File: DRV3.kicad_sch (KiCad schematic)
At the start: 15 parts

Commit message: Motor symbol corrected, Oscillator circuitry added and external footprints added
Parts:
- removed UC: DRV10970PWPR, symbol DRV10970PWPR:DRV10970PWPR
- added UA?: DRV10970PWPR, DRV10970PWPR:SOP65P640X120-25N, symbol DRV10970PWPR:DRV10970PWPR
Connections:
- net BRK_3: now also UA?.21 (BRKMOD)
- net CMT_3: now also UA?.20 (CMTMOD)
- net CPN: now also UA?.10 (CPN)
- net CPP: now also UA?.9 (CPP)
- net CS: now also UA?.17 (CS)
- net FG_3: now also UA?.24 (FG)
- net FR_3: now also UA?.23 (FR)
- net GND: now also UA?.12 (GND), UA?.25 (EP)
- net MOT_POW: now also UA?.15 (VM)
- net MOT_PWM_3: now also UA?.19 (PWM)
- net RD_3: now also UA?.18 (RD)
- net RTRY: now also UA?.22 (RETRY)
- net U_3: now also UA?.14 (U)
- net U_HP_3: now also UA?.2 (U_HP)
- net VCP: now also UA?.8 (VCP)
- net VINT: now also UA?.16 (VINT)
- net VINT_BY_2: now also UA?.3 (U_HN), UA?.5 (V_HN), UA?.7 (W_HN)
- net V_3: now also UA?.13 (V)
- net V_HP_3: now also UA?.4 (V_HP)
- net W_3: now also UA?.11 (W)
- net W_HP_3: now also UA?.6 (W_HP)
- net at TPC1.1: now also UA?.1 (DAA)
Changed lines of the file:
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@@
   (symbol (lib_id "power:GND") (at 181.61 109.22 0) (unit 1)
     (in_bom yes) (on_board yes) (fields_autoplaced)
-    (property "Reference" "#PWR?" (id 0) (at 181.61 115.57 0)
+    (property "Reference" "#PWR0193" (id 0) (at 181.61 115.57 0)
       (effects (font (size 1.27 1.27)) hide)
     )
@@
   (symbol (lib_id "power:GND") (at 215.9 139.7 0) (unit 1)
     (in_bom yes) (on_board yes) (fields_autoplaced)
-    (property "Reference" "#PWR?" (id 0) (at 215.9 146.05 0)
+    (property "Reference" "#PWR0191" (id 0) (at 215.9 146.05 0)
       (effects (font (size 1.27 1.27)) hide)
     )
@@
     (pin "2")
   )
+  (symbol (lib_id "power:GND") (at 198.12 101.6 0) (unit 1)
+    (in_bom yes) (on_board yes) (fields_autoplaced)
+    (property "Reference" "#PWR0192" (id 0) (at 198.12 107.95 0)
+      (effects (font (size 1.27 1.27)) hide)
+    )
+    (property "Value" "GND" (id 1) (at 198.12 106.68 0))
+    (property "Footprint" "" (id 2) (at 198.12 101.6 0)
+      (effects (font (size 1.27 1.27)) hide)
+    )
+    (property "Datasheet" "" (id 3) (at 198.12 101.6 0)
+      (effects (font (size 1.27 1.27)) hide)
+    )
+    (pin "1")
+  )
+  (symbol (lib_id "Device:R") (at 198.12 90.17 0) (unit 1)
+    (in_bom yes) (on_board yes) (fields_autoplaced)
+    (property "Reference" "RC6" (id 0) (at 200.66 88.8999 0)
+      (effects (font (size 1.27 1.27)) (justify left))
+    )
+    (property "Value" "22K" (id 1) (at 200.66 91.4399 0)
+      (effects (font (size 1.27 1.27)) (justify left))
+    )
+    (property "Footprint" "" (id 2) (at 196.342 90.17 90)
+      (effects (font (size 1.27 1.27)) hide)
+    )
+    (property "Datasheet" "~" (id 3) (at 198.12 90.17 0)
+      (effects (font (size 1.27 1.27)) hide)
+    )
+    (pin "1")
+    (pin "2")
+  )
+  (symbol (lib_id "power:GND") (at 130.81 104.14 0) (unit 1)
+    (in_bom yes) (on_board yes) (fields_autoplaced)
+    (property "Reference" "#PWR0188" (id 0) (at 130.81 110.49 0)
+      (effects (font (size 1.27 1.27)) hide)
+    )
+    (property "Value" "GND" (id 1) (at 130.81 109.22 0))
+    (property "Footprint" "" (id 2) (at 130.81 104.14 0)
+      (effects (font (size 1.27 1.27)) hide)
+    )
+    (property "Datasheet" "" (id 3) (at 130.81 104.14 0)
+      (effects (font (size 1.27 1.27)) hide)
+    )
+    (pin "1")
+  )
+  (symbol (lib_id "pspice:C") (at 119.38 139.7 0) (unit 1)
+    (in_bom yes) (on_board yes) (fields_autoplaced)
+    (property "Reference" "CA?" (id 0) (at 124.46 138.4299 0)
+      (effects (font (size 1.27 1.27)) (justify left))
+    )
+    (property "Value" "1u" (id 1) (at 124.46 140.9699 0)
+      (effects (font (size 1.27 1.27)) (justify left))
+    )
+    (property "Footprint" "" (id 2) (at 119.38 139.7 0)
+      (effects (font (size 1.27 1.27)) hide)
+    )
+    (property "Datasheet" "~" (id 3) (at 119.38 139.7 0)
+      (effects (font (size 1.27 1.27)) hide)
+    )
+    (pin "1")
+    (pin "2")
+  )
+  (symbol (lib_id "Device:R") (at 87.63 69.85 0) (unit 1)
+    (in_bom yes) (on_board yes) (fields_autoplaced)
+    (property "Reference" "RC1" (id 0) (at 90.17 68.5799 0)
+      (effects (font (size 1.27 1.27)) (justify left))
+    )
+    (property "Value" "4.7K" (id 1) (at 90.17 71.1199 0)
+      (effects (font (size 1.27 1.27)) (justify left))
+    )
+    (property "Footprint" "" (id 2) (at 85.852 69.85 90)
+      (effects (font (size 1.27 1.27)) hide)
+    )
+    (property "Datasheet" "~" (id 3) (at 87.63 69.85 0)
+      (effects (font (size 1.27 1.27)) hide)
+    )
+    (pin "1")
+    (pin "2")
+  )
+  (symbol (lib_id "Connector:TestPoint") (at 129.54 76.2 0) (unit 1)
+    (in_bom yes) (on_board yes) (fields_autoplaced)
+    (property "Reference" "TPC1" (id 0) (at 132.08 71.6279 0)
+      (effects (font (size 1.27 1.27)) (justify left))
+    )
+    (property "Value" "TestPoint" (id 1) (at 132.08 74.1679 0)
+      (effects (font (size 1.27 1.27)) (justify left))
+    )
+    (property "Footprint" "" (id 2) (at 134.62 76.2 0)
+      (effects (font (size 1.27 1.27)) hide)
+    )
+    (property "Datasheet" "~" (id 3) (at 134.62 76.2 0)
+      (effects (font (size 1.27 1.27)) hide)
+    )
+    (pin "1")
+  )
   (symbol (lib_id "DRV10970PWPR:DRV10970PWPR") (at 130.81 76.2 0) (unit 1)
     (in_bom yes) (on_board yes) (fields_autoplaced)
-    (property "Reference" "UC" (id 0) (at 146.05 63.5 0))
+    (property "Reference" "UA?" (id 0) (at 146.05 63.5 0))
     (property "Value" "DRV10970PWPR" (id 1) (at 146.05 66.04 0))
-    (property "Footprint" "" (id 2) (at 130.81 76.2 0)
+    (property "Footprint" "DRV10970PWPR:SOP65P640X120-25N" (id 2) (at 130.81 76.2 0)
       (effects (font (size 1.27 1.27)) hide)
     )
@@
     (pin "9")
   )
-  (symbol (lib_id "power:GND") (at 198.12 101.6 0) (unit 1)
-    (in_bom yes) (on_board yes) (fields_autoplaced)
-    (property "Reference" "#PWR?" (id 0) (at 198.12 107.95 0)
-      (effects (font (size 1.27 1.27)) hide)
-    )
-    (property "Value" "GND" (id 1) (at 198.12 106.68 0))
-    (property "Footprint" "" (id 2) (at 198.12 101.6 0)
-      (effects (font (size 1.27 1.27)) hide)
-    )
-    (property "Datasheet" "" (id 3) (at 198.12 101.6 0)
-      (effects (font (size 1.27 1.27)) hide)
-    )
-    (pin "1")
-  )
-  (symbol (lib_id "Device:R") (at 198.12 90.17 0) (unit 1)
-    (in_bom yes) (on_board yes) (fields_autoplaced)
-    (property "Reference" "RC6" (id 0) (at 200.66 88.8999 0)
-      (effects (font (size 1.27 1.27)) (justify left))
-    )
-    (property "Value" "22K" (id 1) (at 200.66 91.4399 0)
-      (effects (font (size 1.27 1.27)) (justify left))
-    )
-    (property "Footprint" "" (id 2) (at 196.342 90.17 90)
-      (effects (font (size 1.27 1.27)) hide)
-    )
-    (property "Datasheet" "~" (id 3) (at 198.12 90.17 0)
-      (effects (font (size 1.27 1.27)) hide)
-    )
-    (pin "1")
-    (pin "2")
-  )
-  (symbol (lib_id "power:GND") (at 130.81 104.14 0) (unit 1)
-    (in_bom yes) (on_board yes) (fields_autoplaced)
-    (property "Reference" "#PWR?" (id 0) (at 130.81 110.49 0)
-      (effects (font (size 1.27 1.27)) hide)
-    )
-    (property "Value" "GND" (id 1) (at 130.81 109.22 0))
-    (property "Footprint" "" (id 2) (at 130.81 104.14 0)
-      (effects (font (size 1.27 1.27)) hide)
-    )
-    (property "Datasheet" "" (id 3) (at 130.81 104.14 0)
-      (effects (font (size 1.27 1.27)) hide)
-    )
-    (pin "1")
-  )
-  (symbol (lib_id "pspice:C") (at 119.38 139.7 0) (unit 1)
-    (in_bom yes) (on_board yes) (fields_autoplaced)
-    (property "Reference" "CA?" (id 0) (at 124.46 138.4299 0)
-      (effects (font (size 1.27 1.27)) (justify left))
-    )
-    (property "Value" "1u" (id 1) (at 124.46 140.9699 0)
-      (effects (font (size 1.27 1.27)) (justify left))
-    )
-    (property "Footprint" "" (id 2) (at 119.38 139.7 0)
-      (effects (font (size 1.27 1.27)) hide)
-    )
-    (property "Datasheet" "~" (id 3) (at 119.38 139.7 0)
-      (effects (font (size 1.27 1.27)) hide)
-    )
-    (pin "1")
-    (pin "2")
-  )
-  (symbol (lib_id "Device:R") (at 87.63 69.85 0) (unit 1)
-    (in_bom yes) (on_board yes) (fields_autoplaced)
-    (property "Reference" "RC1" (id 0) (at 90.17 68.5799 0)
-      (effects (font (size 1.27 1.27)) (justify left))
-    )
-    (property "Value" "4.7K" (id 1) (at 90.17 71.1199 0)
-      (effects (font (size 1.27 1.27)) (justify left))
-    )
-    (property "Footprint" "" (id 2) (at 85.852 69.85 90)
-      (effects (font (size 1.27 1.27)) hide)
-    )
-    (property "Datasheet" "~" (id 3) (at 87.63 69.85 0)
-      (effects (font (size 1.27 1.27)) hide)
-    )
-    (pin "1")
-    (pin "2")
-  )
-  (symbol (lib_id "Connector:TestPoint") (at 129.54 76.2 0) (unit 1)
-    (in_bom yes) (on_board yes) (fields_autoplaced)
-    (property "Reference" "TPC1" (id 0) (at 132.08 71.6279 0)
-      (effects (font (size 1.27 1.27)) (justify left))
-    )
-    (property "Value" "TestPoint" (id 1) (at 132.08 74.1679 0)
-      (effects (font (size 1.27 1.27)) (justify left))
-    )
-    (property "Footprint" "" (id 2) (at 134.62 76.2 0)
-      (effects (font (size 1.27 1.27)) hide)
-    )
-    (property "Datasheet" "~" (id 3) (at 134.62 76.2 0)
-      (effects (font (size 1.27 1.27)) hide)
-    )
-    (pin "1")
-  )
   (symbol (lib_id "pspice:C") (at 181.61 102.87 0) (unit 1)
     (in_bom yes) (on_board yes) (fields_autoplaced)
@@
   (symbol (lib_id "power:GND") (at 147.32 146.685 0) (unit 1)
     (in_bom yes) (on_board yes)
-    (property "Reference" "#PWR?" (id 0) (at 147.32 153.035 0)
+    (property "Reference" "#PWR0190" (id 0) (at 147.32 153.035 0)
       (effects (font (size 1.27 1.27)) hide)
     )
@@
   (symbol (lib_id "power:GND") (at 146.05 116.84 0) (unit 1)
     (in_bom yes) (on_board yes) (fields_autoplaced)
-    (property "Reference" "#PWR?" (id 0) (at 146.05 123.19 0)
-      (effects (font (size 1.27 1.27)) hide)
-    )
+    (property "Reference" "#PWR0189" (id 0) (at 146.05 123.19 0)
+      (effects (font (size 1.27 1.27)) hide)
+    )

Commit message: MCU interfaces are done! Check the Changes and Complete ERC modifications
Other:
- company: (none) -> Parikshit Student Satellite Team
- title: (none) -> AOCS BOARD
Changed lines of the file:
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@@
 (kicad_sch (version 20211123) (generator eeschema)
   (paper "A4")
+  (title_block
+    (title "AOCS BOARD")
+    (company "Parikshit Student Satellite Team")
+  )
   (junction (at 99.06 66.04) (diameter 0) (color 0 0 0 0)
   )
@@
   )
   (wire (pts (xy 176.53 86.36) (xy 176.53 91.44))
+    (stroke (width 0) (type default) (color 0 0 0 0))
+  )
+  (wire (pts (xy 31.115 144.145) (xy 31.115 142.875))
     (stroke (width 0) (type default) (color 0 0 0 0))
   )
@@
     (pin "1")
     (pin "2")
+  )
+  (symbol (lib_id "power:GND") (at 31.115 144.145 0) (unit 1)
+    (in_bom yes) (on_board yes) (fields_autoplaced)
+    (property "Reference" "#PWR0274" (id 0) (at 31.115 150.495 0)
+      (effects (font (size 1.27 1.27)) hide)
+    )
+    (property "Value" "GND" (id 1) (at 31.115 148.59 0))
+    (property "Footprint" "" (id 2) (at 31.115 144.145 0)
+      (effects (font (size 1.27 1.27)) hide)
+    )
+    (property "Datasheet" "" (id 3) (at 31.115 144.145 0)
+      (effects (font (size 1.27 1.27)) hide)
+    )
+    (pin "1")
   )
   (symbol (lib_id "Device:R") (at 163.83 69.85 0) (unit 1)
@@
     (pin "2")
   )
+  (symbol (lib_id "power:PWR_FLAG") (at 31.115 142.875 0) (unit 1)
+    (in_bom yes) (on_board yes) (fields_autoplaced)
+    (property "Reference" "#FLG0110" (id 0) (at 31.115 140.97 0)
+      (effects (font (size 1.27 1.27)) hide)
+    )
+    (property "Value" "PWR_FLAG" (id 1) (at 31.115 137.16 0))
+    (property "Footprint" "" (id 2) (at 31.115 142.875 0)
+      (effects (font (size 1.27 1.27)) hide)
+    )
+    (property "Datasheet" "~" (id 3) (at 31.115 142.875 0)
+      (effects (font (size 1.27 1.27)) hide)
+    )
+    (pin "1")
+  )
 )

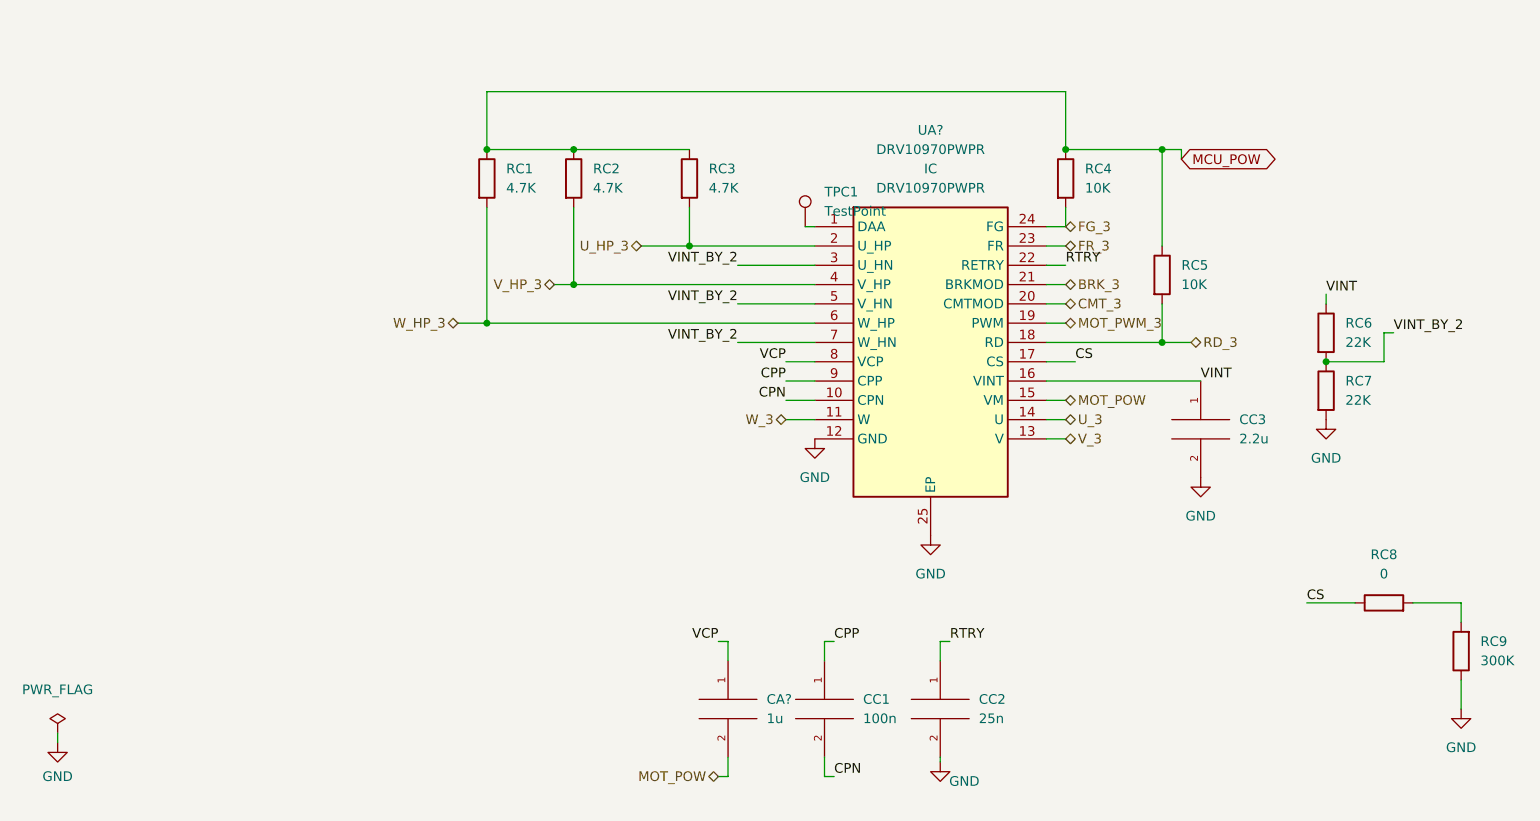
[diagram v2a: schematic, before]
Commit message: Max ERC errors corrected
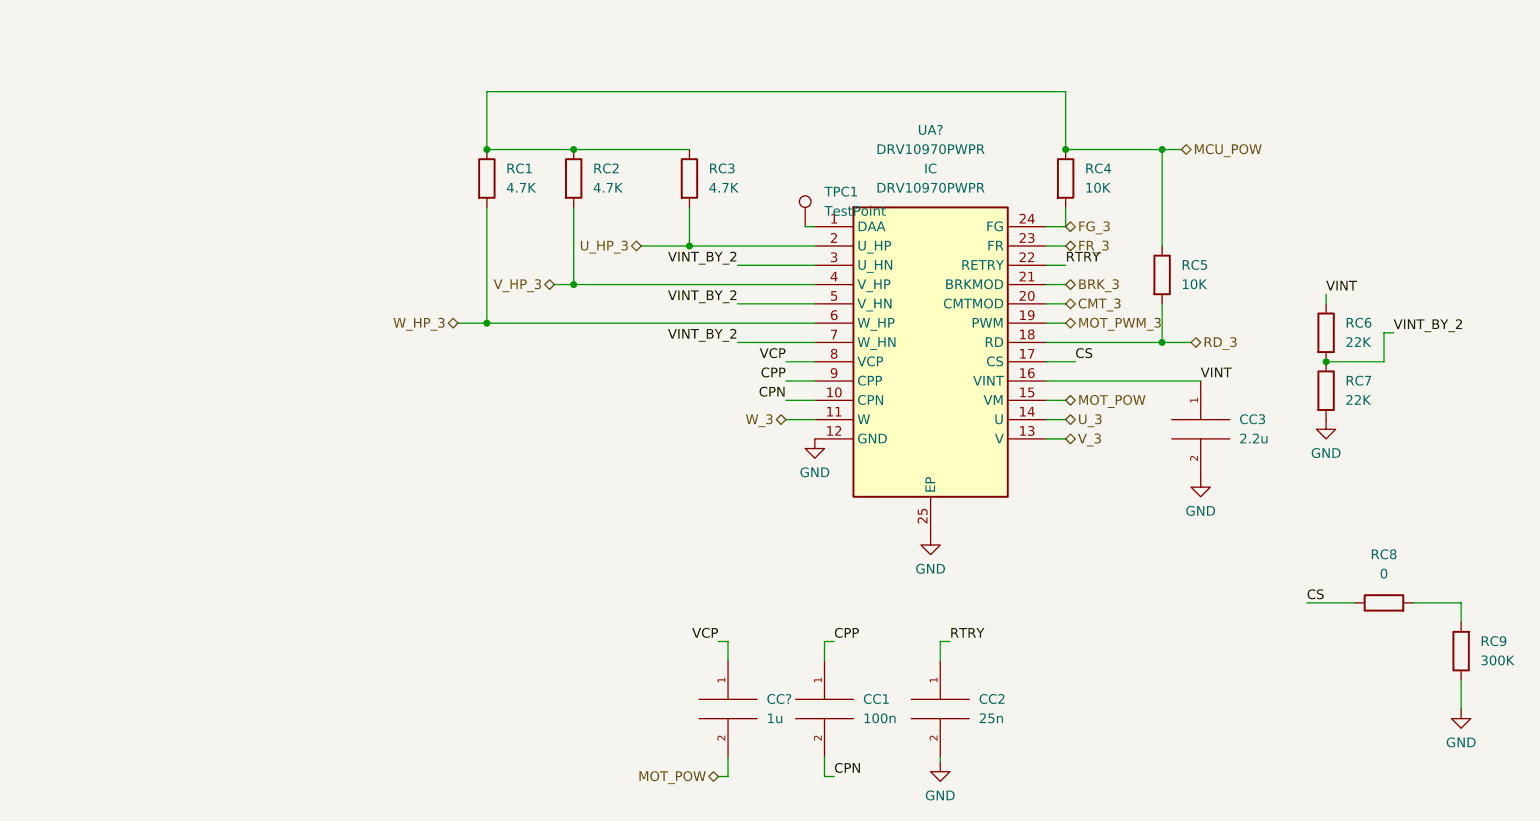
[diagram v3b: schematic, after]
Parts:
- gave numbers to parts that had none: 1

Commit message: Updated the changes
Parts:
- gave numbers to parts that had none: 2
- renumbered CC3 to CC1, CC1 to CC3, CC2 to CC4
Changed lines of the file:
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@@
   (symbol (lib_id "upsat-comms-hardware:GND") (at 181.61 109.22 0) (unit 1)
     (in_bom yes) (on_board yes) (fields_autoplaced)
-    (property "Reference" "#PWR0193" (id 0) (at 181.61 115.57 0)
+    (property "Reference" "#PWR093" (id 0) (at 181.61 115.57 0)
       (effects (font (size 1.27 1.27)) hide)
     )
@@
   (symbol (lib_id "upsat-comms-hardware:GND") (at 130.81 104.14 0) (unit 1)
     (in_bom yes) (on_board yes) (fields_autoplaced)
-    (property "Reference" "#PWR0188" (id 0) (at 130.81 110.49 0)
+    (property "Reference" "#PWR092" (id 0) (at 130.81 110.49 0)
       (effects (font (size 1.27 1.27)) hide)
     )
@@
   (symbol (lib_id "pspice:C") (at 132.08 139.7 0) (unit 1)
     (in_bom yes) (on_board yes) (fields_autoplaced)
-    (property "Reference" "CC1" (id 0) (at 137.16 138.4299 0)
+    (property "Reference" "CC3" (id 0) (at 137.16 138.4299 0)
       (effects (font (size 1.27 1.27)) (justify left))
     )
@@
   (symbol (lib_id "upsat-comms-hardware:GND") (at 215.9 139.7 0) (unit 1)
     (in_bom yes) (on_board yes) (fields_autoplaced)
-    (property "Reference" "#PWR0191" (id 0) (at 215.9 146.05 0)
+    (property "Reference" "#PWR095" (id 0) (at 215.9 146.05 0)
       (effects (font (size 1.27 1.27)) hide)
     )
@@
   (symbol (lib_id "pspice:C") (at 147.32 139.7 0) (unit 1)
     (in_bom yes) (on_board yes) (fields_autoplaced)
-    (property "Reference" "CC2" (id 0) (at 152.4 138.4299 0)
+    (property "Reference" "CC4" (id 0) (at 152.4 138.4299 0)
       (effects (font (size 1.27 1.27)) (justify left))
     )
@@
   (symbol (lib_id "pspice:C") (at 119.38 139.7 0) (unit 1)
     (in_bom yes) (on_board yes) (fields_autoplaced)
-    (property "Reference" "CC?" (id 0) (at 124.46 138.4299 0)
+    (property "Reference" "CC2" (id 0) (at 124.46 138.4299 0)
       (effects (font (size 1.27 1.27)) (justify left))
     )
@@
   (symbol (lib_id "upsat-comms-hardware:GND") (at 146.05 116.84 0) (unit 1)
     (in_bom yes) (on_board yes) (fields_autoplaced)
-    (property "Reference" "#PWR0189" (id 0) (at 146.05 123.19 0)
+    (property "Reference" "#PWR094" (id 0) (at 146.05 123.19 0)
       (effects (font (size 1.27 1.27)) hide)
     )
@@
   (symbol (lib_id "upsat-comms-hardware:GND") (at 198.12 101.6 0) (unit 1)
     (in_bom yes) (on_board yes) (fields_autoplaced)
-    (property "Reference" "#PWR0192" (id 0) (at 198.12 107.95 0)
+    (property "Reference" "#PWR091" (id 0) (at 198.12 107.95 0)
       (effects (font (size 1.27 1.27)) hide)
     )
@@
   (symbol (lib_id "upsat-comms-hardware:GND") (at 147.32 146.685 0) (unit 1)
     (in_bom yes) (on_board yes) (fields_autoplaced)
-    (property "Reference" "#PWR0190" (id 0) (at 147.32 153.035 0)
+    (property "Reference" "#PWR096" (id 0) (at 147.32 153.035 0)
       (effects (font (size 1.27 1.27)) hide)
     )
@@
   (symbol (lib_id "DRV10970PWPR:DRV10970PWPR") (at 130.81 76.2 0) (unit 1)
     (in_bom yes) (on_board yes) (fields_autoplaced)
-    (property "Reference" "UA?" (id 0) (at 146.05 63.5 0))
+    (property "Reference" "UA3" (id 0) (at 146.05 63.5 0))
     (property "Value" "DRV10970PWPR" (id 1) (at 146.05 66.04 0))
     (property "Footprint" "DRV10970PWPR:SOP65P640X120-25N" (id 2) (at 130.81 76.2 0)
@@
   (symbol (lib_id "pspice:C") (at 181.61 102.87 0) (unit 1)
     (in_bom yes) (on_board yes) (fields_autoplaced)
-    (property "Reference" "CC3" (id 0) (at 186.69 101.5999 0)
-      (effects (font (size 1.27 1.27)) (justify left))
-    )
+    (property "Reference" "CC1" (id 0) (at 186.69 101.5999 0)
+      (effects (font (size 1.27 1.27)) (justify left))
+    )

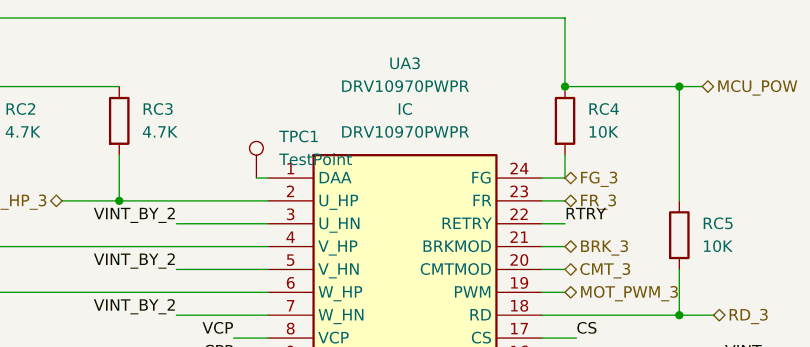
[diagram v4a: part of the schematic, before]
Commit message: Placed NCs at ADCS_HMC1051
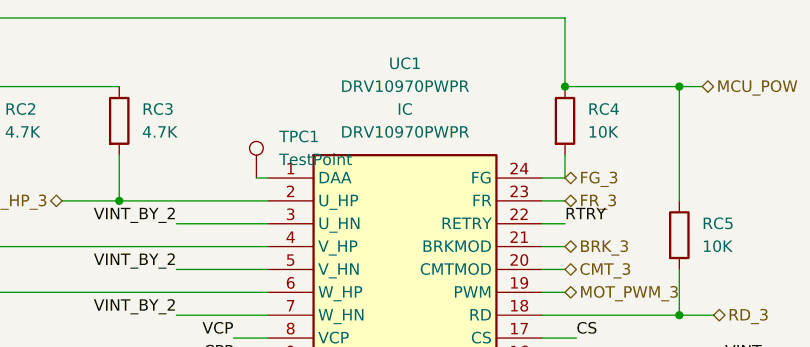
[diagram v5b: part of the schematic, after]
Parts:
- renumbered UA3 to UC1
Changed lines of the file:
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@@
   (symbol (lib_id "DRV10970PWPR:DRV10970PWPR") (at 130.81 76.2 0) (unit 1)
     (in_bom yes) (on_board yes) (fields_autoplaced)
-    (property "Reference" "UA3" (id 0) (at 146.05 63.5 0))
+    (property "Reference" "UC1" (id 0) (at 146.05 63.5 0))
     (property "Value" "DRV10970PWPR" (id 1) (at 146.05 66.04 0))
     (property "Footprint" "DRV10970PWPR:SOP65P640X120-25N" (id 2) (at 130.81 76.2 0)
